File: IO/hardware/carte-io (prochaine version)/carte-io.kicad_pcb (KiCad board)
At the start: 4 copper layers, 117.5 x 88.5 mm, 180 parts, among them J1 USB_C_Receptacle_USB2.0_14P, J10 114020164, J11 114020164, J12 114020164, J13 114020164, J14 114020164, J15 114020164, J16 114020164, J17 114020164, J18 114020164, J19 114020164, J2 114020164, J20 114020164, J21 114020164, J22 114020164, J23 114020164, J24 114020164, J25 114020164, J26 114020164, J27 114020164, J28 114020164, J29 114020164, J3 FTSH-105-01-L-DH, J30 114020164, J4 114020164, J5 114020164, J6 114020164, J7 114020164, J8 TSW-104-07-G-T, J9 TSW-104-07-G-T, Q1 IRF9388TRPBF, SW1 SW_Push, SW2 SW_Push, U1 STM32U545VETx, U10 CM1293A-04SO, U11 74LVC125APW, U12 LSM6DS3, U13 LIS2MDL, U14 LPS22DF, U15 PCA9544APW, U16 LT1963AxST-3.3, U17 PCA9544APW, U18 APDS-9251-001, U19 SHT4x, U2 FT231XQ, U20 74LVC2G125DP,125, U21 CM1293A-04SO, U24 CM1293A-04SO, U26 74LVC2G125DP,125, U27 CM1293A-04SO, U28 74LVC2G125DP,125, U29 CM1293A-04SO, U3 LT1963AxST-3.3, U33 MCP2542FDxMF, U35 TCA9802, U4 CM1293A-04SO, U5 TXU0104PWR, U6 74LVC125APW, U7 CM1293A-04SO, U8 CM1293A-04SO, U9 TXU0104PWR, X1 ASE-16.000MHZ-LC-T

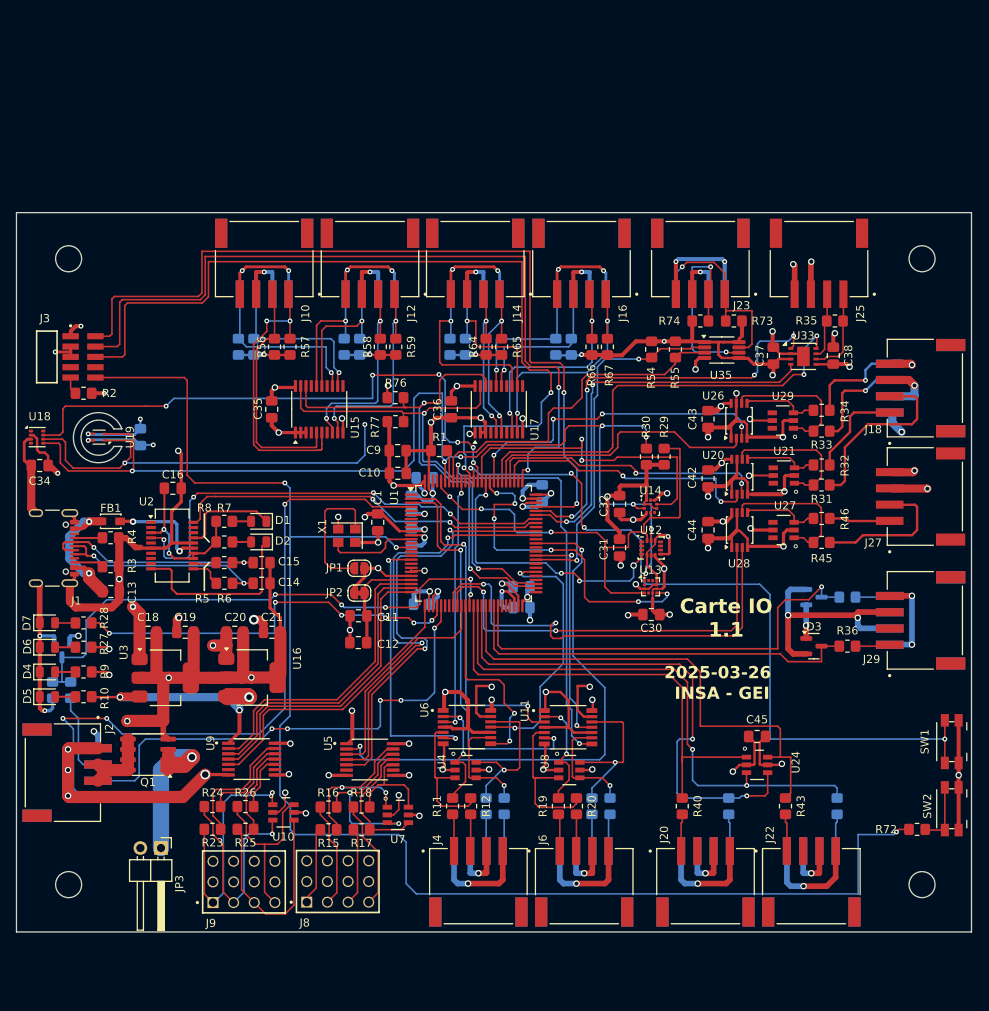
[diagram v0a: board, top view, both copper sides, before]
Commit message: Recuperation de la carte IO perdue lors de la suppression des 3 derniers commit
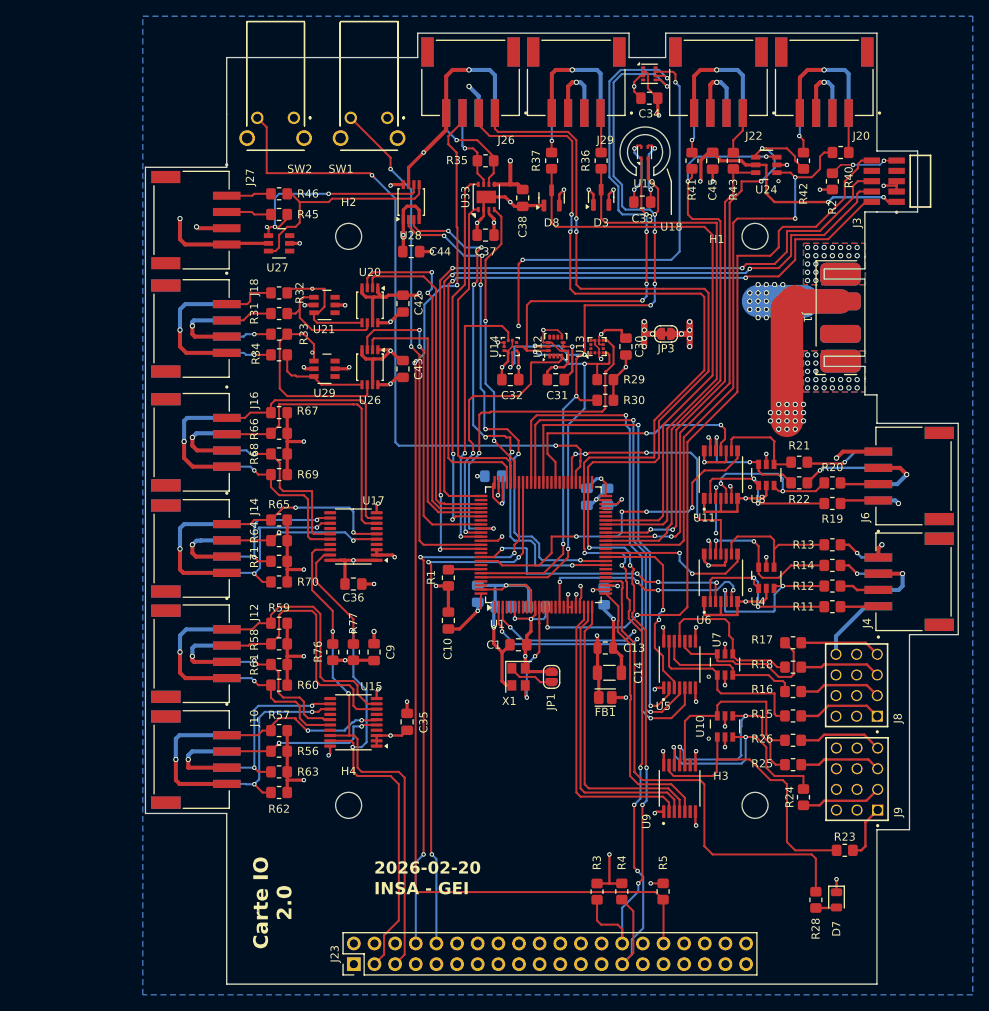
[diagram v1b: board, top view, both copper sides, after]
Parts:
- removed C11, C18, C20: 100nF, Capacitor_SMD:C_0805_2012Metric_Pad1.18x1.45mm_HandSolder
- removed C12: 1µF, Capacitor_SMD:C_0805_2012Metric_Pad1.18x1.45mm_HandSolder
- removed C15: 47pF, Capacitor_SMD:C_0805_2012Metric_Pad1.18x1.45mm_HandSolder
- removed C16: 10nf, Capacitor_SMD:C_0805_2012Metric_Pad1.18x1.45mm_HandSolder
- removed C19, C21: 10µF, Capacitor_SMD:C_0805_2012Metric_Pad1.18x1.45mm_HandSolder
- removed D1, D2, D4, D5, D6: LED, LED_SMD:LED_0805_2012Metric
- removed D9: BAT54SFILMY, Package_TO_SOT_SMD:SOT-23
- removed J2, J24: 114020164, SeeedStudio - Horizontal Header -114020164:SEEEDSTUDIO_114020164
- removed JP2: SolderJumper_2_Bridged, Jumper:SolderJumper-2_P1.3mm_Bridged_RoundedPad1.0x1.5mm
- removed Q1: IRF9388TRPBF, Package_SO:SOIC-8_3.9x4.9mm_P1.27mm
- removed R10, R27, R7, R8: 150R, Resistor_SMD:R_0805_2012Metric_Pad1.20x1.40mm_HandSolder
- removed R52, R53: 100R, Resistor_SMD:R_0805_2012Metric_Pad1.20x1.40mm_HandSolder
- removed R54, R55, R73, R74: 4.7K, Resistor_SMD:R_0805_2012Metric_Pad1.20x1.40mm_HandSolder
- removed R6: 27R, Resistor_SMD:R_0805_2012Metric_Pad1.20x1.40mm_HandSolder
- removed R72: 10K, Resistor_SMD:R_0805_2012Metric_Pad1.20x1.40mm_HandSolder
- removed R9: 330R, Resistor_SMD:R_0805_2012Metric_Pad1.20x1.40mm_HandSolder
- removed U16, U3: LT1963AxST-3.3, Package_TO_SOT_SMD:SOT-223-3_TabPin2
- removed U2: FT231XQ, Package_SO:SSOP-20_3.9x8.7mm_P0.635mm
- removed U35: TCA9802, Package_SO:VSSOP-8_3x3mm_P0.65mm
- C13: value 10nF -> 100nF; footprint Capacitor_SMD:C_0805_2012Metric_Pad1.18x1.45mm_HandSolder -> Capacitor_SMD:C_0805_2012Metric
- C14: value 47pF -> 10µF; footprint Capacitor_SMD:C_0805_2012Metric_Pad1.18x1.45mm_HandSolder -> Capacitor_SMD:C_1206_3216Metric
- C33, D8, J26, R13, R14, R21, R22, R37, R41, R42, R60, R61, R62, R63, R68, R69, R70, R71: moved to F.Cu
- FB1: value FerriteBead_Small -> MZ2029-601Y; footprint Inductor_SMD:L_Walsin_WLFM201209x -> Inductor_SMD:L_Eaton_MCL2012V1
- J1: value USB_C_Receptacle_USB2.0_14P -> Multiplex MPX 6; footprint Connector_USB:USB_C_Receptacle_GCT_USB4105-xx-A_16P_TopMnt_Horizontal -> Multiplex MPX 6:MPX6
- J23: value 114020164 -> Connecteur JETSON; footprint SeeedStudio - Horizontal Header -114020164:SEEEDSTUDIO_114020164 -> Connector_PinHeader_2.54mm:PinHeader_2x20_P2.54mm_Vertical
- J25: moved to B.Cu
- JP3: value Jumper_2_Bridged -> SolderJumper_2_Bridged; footprint Connector_PinHeader_2.54mm:PinHeader_1x02_P2.54mm_Horizontal -> Jumper:SolderJumper-2_P1.3mm_Bridged_RoundedPad1.0x1.5mm
- R3, R4: value 5.1K -> 4.7K
- R5: value 27R -> 4.7K
- SW1, SW2: footprint Button_Switch_SMD:Panasonic_EVQPUJ_EVQPUA -> 2-1825027-0:218250270
- moved SW2 117.4 mm to (121.7, 43.7), turned to 180 degrees
- moved J1 104.3 mm to (191.5, 68.2), turned to 90 degrees
- moved SW1 103.5 mm to (133.2, 43.7), turned to 180 degrees
- moved D7 102.9 mm to (188.5, 139.9), turned to -90 degrees
- moved J3 100.9 mm to (194.3, 51.5), turned to -90 degrees
- moved J20 100.5 mm to (187.0, 38.7), turned to 180 degrees
- moved J21 100.5 mm to (187.0, 38.7), turned to 0 degrees
- moved J22 100.1 mm to (173.9, 38.7), turned to 180 degrees
- moved J28 100.1 mm to (173.9, 38.7), turned to 0 degrees
- moved J26 99.1 mm to (143.4, 38.7), turned to 180 degrees
- moved J23 96.7 mm to (129.1, 147.8), turned to 90 degrees
- moved J27 96.4 mm to (109.1, 56.2), turned to -90 degrees
- moved R28 96.3 mm to (185.9, 139.9), turned to -90 degrees
- moved R2 95.7 mm to (188.0, 51.5), turned to -90 degrees
- moved J18 90.5 mm to (109.1, 69.6), turned to -90 degrees
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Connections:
- net /CPU/USER_BTN renamed /CPU/USER_BTN_1
- C13 pad 1: VBUS -> VDDA
- C14 pad 1: /Power & Analog/USB-DP -> VDDA
- FB1 pad 1: VBUS -> +3.3V
- FB1 pad 2: /Power & Analog/FT231_VCC -> VDDA
- J20 pad 3: +3.3V -> +3.3V_PWR
- J21 pad 3: +3.3V -> +3.3V_PWR
- J22 pad 3: +3.3V -> +3.3V_PWR
- J23 pad 1: Net-(J23-Pin_1) -> unconnected-(J23-Pin_1-Pad1)
- J23 pad 2: Net-(J23-Pin_2) -> unconnected-(J23-Pin_2-Pad2)
- J23 pad 3: +3.3V_PWR -> /Externals I2C/SENSORS_I2C_SDA
- J23 pad 4: GND -> unconnected-(J23-Pin_4-Pad4)
- J26 pad 1: /CPU/~{POWEROFF} -> /Jetson-Alimentation/JETSON_I2C0_SCL
- J26 pad 2: /CPU/PWR_CSLEEP -> /Jetson-Alimentation/JETSON_I2C0_SDA
- J26 pad 3: Net-(J26-Pin_3) -> /Jetson-Alimentation/OBC_SHUTDOWN
- J28 pad 3: +3.3V -> +3.3V_PWR
- J29 pad 3: +3.3V -> +3.3V_PWR
- J30 pad 3: +3.3V -> +3.3V_PWR
- J4 pad 3: +3.3V -> +3.3V_PWR
- J5 pad 3: +3.3V -> +3.3V_PWR
- J6 pad 3: +3.3V -> +3.3V_PWR
- J7 pad 3: +3.3V -> +3.3V_PWR
- J8 pad 02: +5V -> +6V
- J8 pad 05: +5V -> +6V
- J8 pad 08: +5V -> +6V
- J8 pad 11: +5V -> +6V
- J9 pad 01: Net-(U10-CH1) -> Net-(J9-Pad01)
- J9 pad 02: +5V -> unconnected-(J9-Pad02)
- J9 pad 04: Net-(U10-CH2) -> Net-(J9-Pad04)
- J9 pad 05: +5V -> unconnected-(J9-Pad05)
- J9 pad 07: Net-(U10-CH3) -> Net-(J9-Pad07)
- J9 pad 08: +5V -> unconnected-(J9-Pad08)
- J9 pad 10: Net-(U10-CH4) -> Net-(J9-Pad10)
- J9 pad 11: +5V -> unconnected-(J9-Pad11)
- JP3 pad 1: Net-(JP3-A) -> +3.3V_PWR
- JP3 pad 2: +5V -> +3.3V
- R23 pad 1: Net-(U9-B1Y) -> Net-(U10-CH1)
- R23 pad 2: Net-(U10-CH1) -> Net-(J9-Pad01)
- R24 pad 1: Net-(U9-B2Y) -> Net-(U10-CH2)
- R24 pad 2: Net-(U10-CH2) -> Net-(J9-Pad04)
- R25 pad 1: Net-(U9-B3Y) -> Net-(U10-CH3)
- R25 pad 2: Net-(U10-CH3) -> Net-(J9-Pad07)
- R26 pad 1: Net-(U9-B4Y) -> Net-(U10-CH4)
- R26 pad 2: Net-(U10-CH4) -> Net-(J9-Pad10)
- R3 pad 1: Net-(J1-CC2) -> +3.3V
- R3 pad 2: GND -> /Jetson-Alimentation/JETSON_I2C0_SCL
- R4 pad 1: Net-(J1-CC1) -> +3.3V
- R4 pad 2: GND -> /Jetson-Alimentation/JETSON_I2C0_SDA
- R5 pad 1: /Power & Analog/USB-DN -> /Jetson-Alimentation/OBC_SHUTDOWN
- R5 pad 2: /Power & Analog/USB2-DN -> GND
- R76 pad 2: /CPU/I2C_SCL_EXTERNAL -> /Externals I2C/SENSORS_I2C_SCL
- R77 pad 2: /CPU/I2C_SDA_EXTERNAL -> /Externals I2C/SENSORS_I2C_SDA
- SW2 pad 2: Net-(R72-Pad2) -> /CPU/USER_BTN_2
- U1 pad 15: /CPU/COM_EXT_RX -> unconnected-(U1-PC0-Pad15)
- U1 pad 16: /CPU/COM_EXT_TX -> unconnected-(U1-PC1-Pad16)
- U1 pad 18: /CPU/US_PulseStart -> unconnected-(U1-PC3-Pad18)
- U1 pad 30: /CPU/PWR_CSLEEP -> unconnected-(U1-PA5-Pad30)
- U1 pad 37: /CPU/ADC_VBAT -> unconnected-(U1-PB2-Pad37)
- U1 pad 4: /CPU/~{POWEROFF} -> unconnected-(U1-PE5-Pad4)
- U1 pad 52: /CPU/I2C_SCL_EXTERNAL -> /Jetson-Alimentation/JETSON_I2C0_SCL
- U1 pad 53: /CPU/I2C_SDA_EXTERNAL -> /Jetson-Alimentation/JETSON_I2C0_SDA
- U1 pad 55: unconnected-(U1-PD8-Pad55) -> /CPU/USER_BTN_2
- U1 pad 59: /CPU/I2C_SCL_ARBITRARY -> unconnected-(U1-PD12-Pad59)
- U1 pad 62: /CPU/US_PulseEnd -> unconnected-(U1-PD15-Pad62)
- U1 pad 68: /CPU/COM_USB_TX -> /CPU/COM_TXD_IO
- U1 pad 69: /CPU/COM_USB_RX -> /CPU/COM_RXD_IO
- U1 pad 93: /CPU/I2C_SDA_ARBITRARY -> unconnected-(U1-PB7-Pad93)
- U15 pad 18: /CPU/I2C_SCL_EXTERNAL -> /Externals I2C/SENSORS_I2C_SCL
- U15 pad 19: /CPU/I2C_SDA_EXTERNAL -> /Externals I2C/SENSORS_I2C_SDA
- U17 pad 18: /CPU/I2C_SCL_EXTERNAL -> /Externals I2C/SENSORS_I2C_SCL
- U17 pad 19: /CPU/I2C_SDA_EXTERNAL -> /Externals I2C/SENSORS_I2C_SDA
- U9 pad 10: Net-(U9-B4Y) -> Net-(U10-CH4)
- U9 pad 11: Net-(U9-B3Y) -> Net-(U10-CH3)
- U9 pad 12: Net-(U9-B2Y) -> Net-(U10-CH2)
- U9 pad 13: Net-(U9-B1Y) -> Net-(U10-CH1)
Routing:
- net GND: track 556.9 -> 394.8 mm, vias 78 -> 98
- net /Jetson-Alimentation/JETSON_I2C0_SDA: track 0.00 -> 159.1 mm, vias 0 -> 7
- net /Jetson-Alimentation/JETSON_I2C0_SCL: track 0.00 -> 152.8 mm, vias 0 -> 7
- net +3.3V: track 398.7 -> 246.0 mm
- net /Jetson-Alimentation/OBC_SHUTDOWN: track 0.00 -> 136.5 mm, vias 0 -> 2
- net +5V: track 201.0 -> 77.0 mm, vias 10 -> 23
- net /CPU/NRST: track 186.8 -> 90.6 mm, vias 3 -> 2
- net /CPU/~{POWEROFF}: track 83.3 -> 0.00 mm, vias 3 -> 0
- net /CPU/USER_BTN_2: track 0.00 -> 82.2 mm, vias 0 -> 2
- net +6V: track 0.00 -> 77.6 mm, vias 0 -> 17
- net /CPU/COM_RXD_IO: track 0.00 -> 68.8 mm, vias 0 -> 3
- net /CPU/COM_TXD_IO: track 0.00 -> 68.1 mm, vias 0 -> 3
- net /CPU/ADC_VBAT: track 67.7 -> 0.00 mm, vias 5 -> 0
- net /Externals I2C/SENSORS_I2C_SDA: track 0.00 -> 66.4 mm, vias 0 -> 2
- net /Externals I2C/SENSORS_I2C_SCL: track 0.00 -> 65.1 mm, vias 0 -> 2
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- added copper zone on In1.Cu, net +3.3V
- added copper zone on B.Cu, net +3.3V_PWR
- added copper zone on In1.Cu, net +5V
- added copper zone on B.Cu, net GND
- added copper zone on F.Cu, net GND
- added copper zone on In2.Cu, net GND
- removed copper zone on In2.Cu, net +3.3V
- removed copper zone on In2.Cu, net +3.3V_PWR
- removed copper zone on In2.Cu, net +5V
- removed copper zone on In1.Cu, net GND
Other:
- board size 117.5 x 88.5 mm -> 100 x 117 mm
